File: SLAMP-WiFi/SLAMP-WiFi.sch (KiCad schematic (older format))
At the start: 19 parts

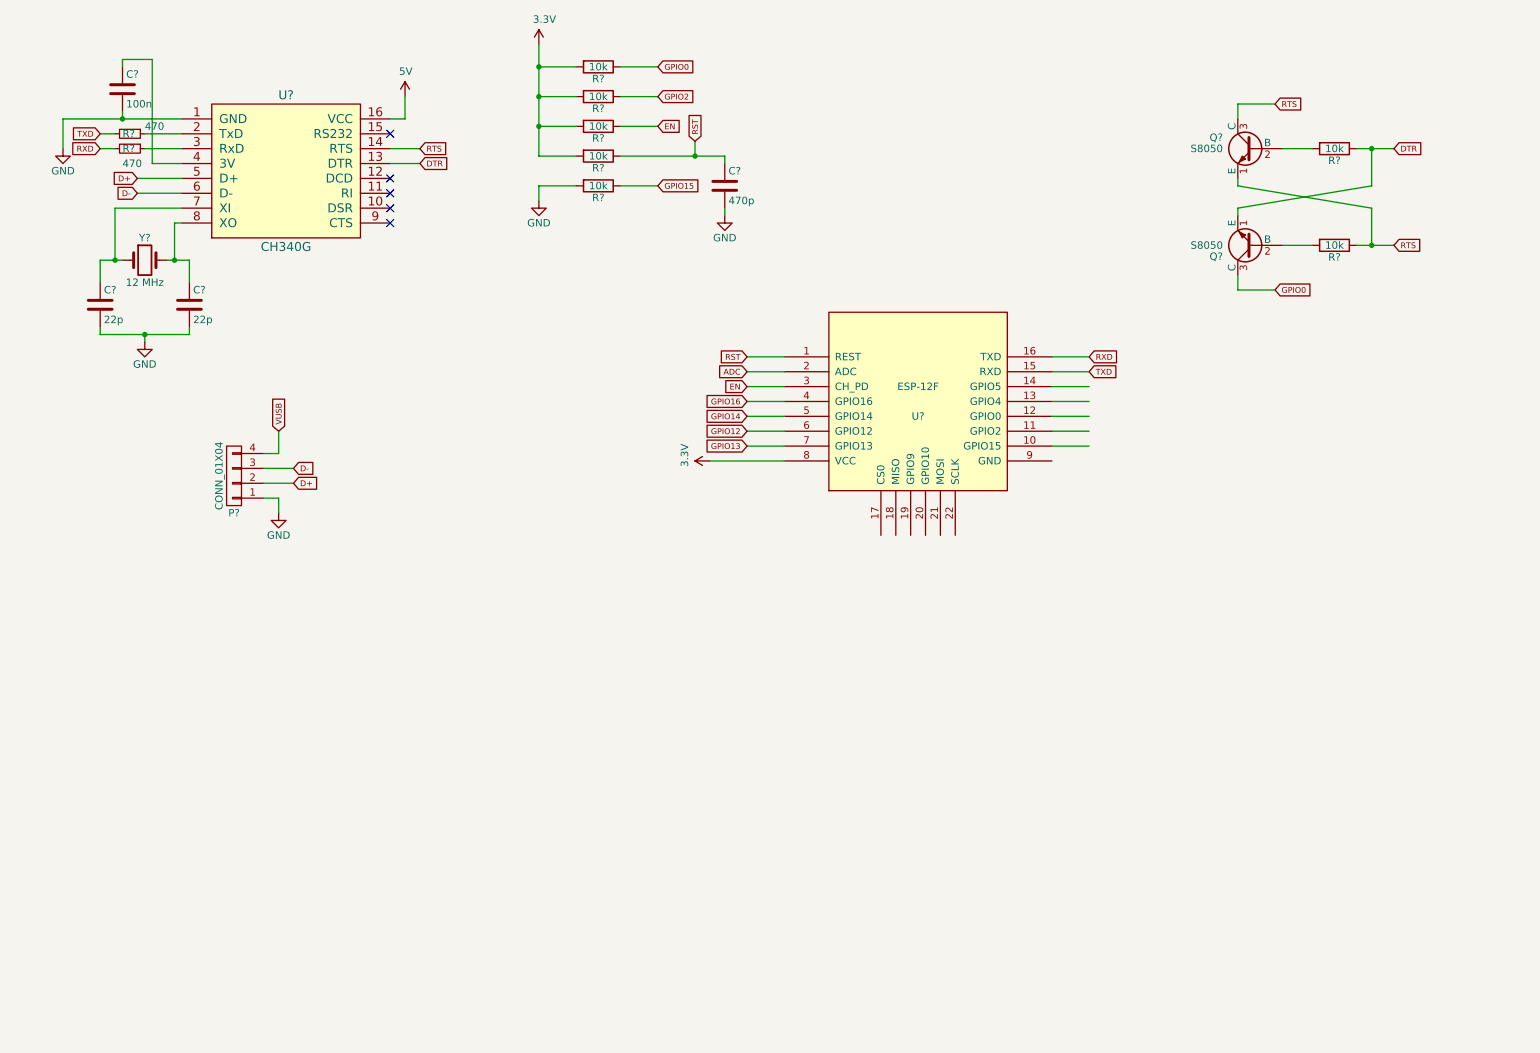
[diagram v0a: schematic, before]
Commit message: Pines de conexionado a las cara terminado, botones terminados
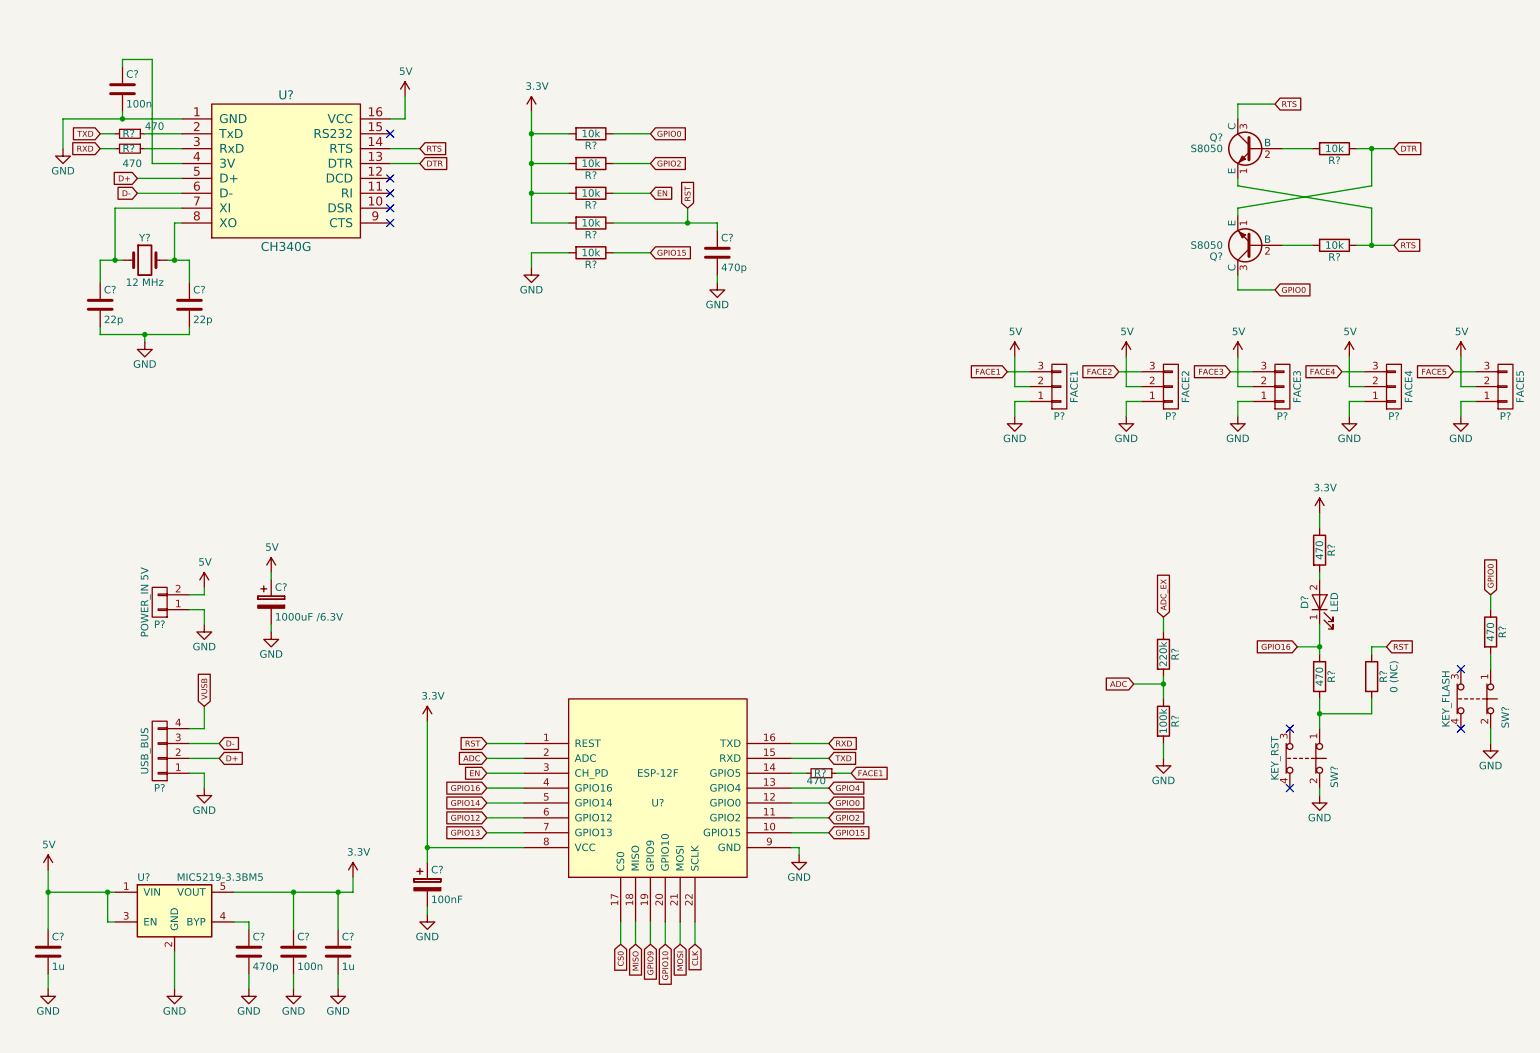
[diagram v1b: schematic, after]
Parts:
- added C?: 470p, symbol C
- added C?: 100n, symbol C
- added C? (x2): 1u, symbol C
- added C?: 100nF, symbol CP
- added C?: 1000uF /6.3V, symbol CP
- added D?: LED, symbol LED
- added P?: POWER_IN 5V, symbol CONN_01X02
- added P?: FACE1, symbol CONN_01X03
- added P?: FACE2, symbol CONN_01X03
- added P?: FACE3, symbol CONN_01X03
- added P?: FACE4, symbol CONN_01X03
- added P?: FACE5, symbol CONN_01X03
- added R?: 100k, symbol R
- added R?: 220k, symbol R
- added R? (x3): 470, symbol R
- added R?: 0 (NC), symbol R
- added R?: 470, symbol R_Small
- added SW?: KEY_RST, symbol SW_Push_Open_Dual
- added SW?: KEY_FLASH, symbol SW_Push_Open_Dual
- added U?: MIC5219-3.3BM5, TO_SOT_Packages_SMD:SOT-23-5, symbol MIC5219-3.3BM5
- P?: value CONN_01X04 -> USB_BUS
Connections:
- net labels added: ADC_EX, CLK, CS0, FACE1, FACE2, FACE3, FACE4, FACE5, GPIO10, GPIO4, GPIO9, MISO, MOSI
- wire segments 79 -> 153
- no-connect marks 5 -> 9
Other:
- moved on the sheet: C?, P?, R?, U?

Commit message: Anotaciones y flags añadidos
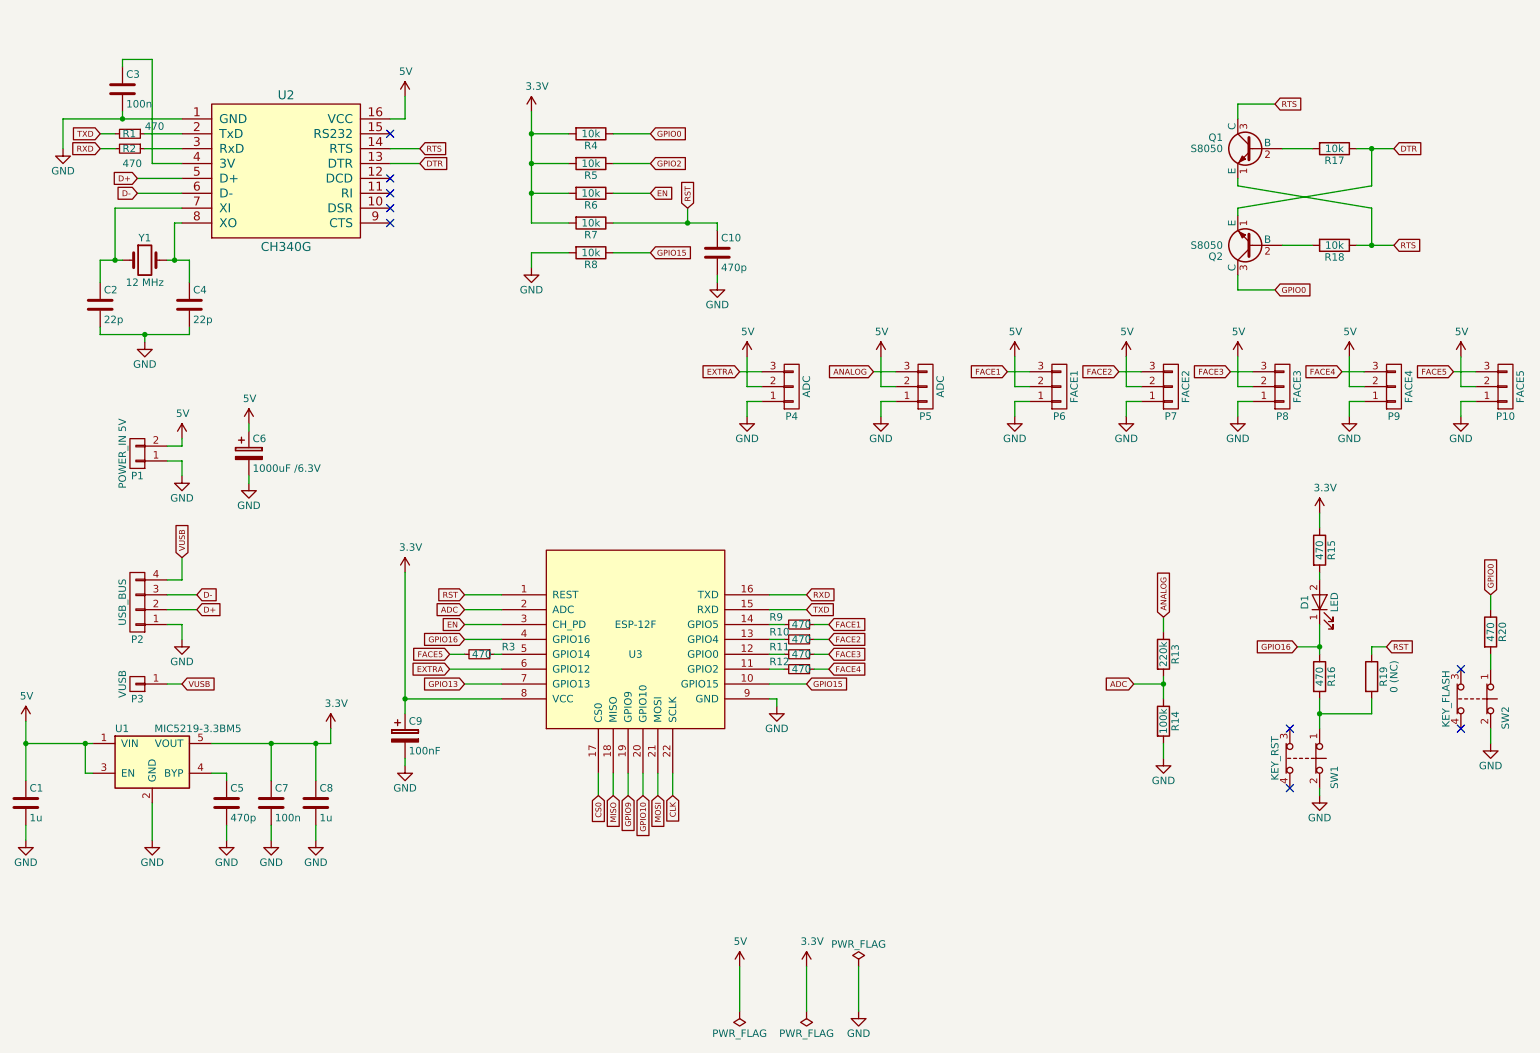
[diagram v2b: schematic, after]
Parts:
- added P3: VUSB, symbol CONN_01X01
- added P4, P5: ADC, symbol CONN_01X03
- added R10, R11, R12, R3: 470, symbol R_Small
- gave numbers to parts that had none: 42
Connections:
- net 5V: now also P4.2 (P2), P5.2 (P2)
- net FACE2: now also R10.1
- net FACE3: now also R11.1
- net FACE4: now also R12.1
- net FACE5: now also R3.2
- net GND: now also P4.1 (P1), P5.1 (P1)
- net GPIO0: no longer U3.12 (GPIO0)
- net GPIO2: no longer U3.11 (GPIO2)
- net VUSB: now also P3.1 (P1)
- net ADC_EX renamed ANALOG
- net ANALOG: now also P5.3 (P3)
- net GPIO12 renamed EXTRA
- net EXTRA: now also P4.3 (P3)
- net GPIO14: no longer names the net of U3.5 (GPIO14)
- net GPIO14: now also R3.1
- net GPIO4: no longer names the net of U3.13 (GPIO4)
- net GPIO4: now also R10.2
- new net: R12.2, U3.11 (GPIO2)
- new net: R11.2, U3.12 (GPIO0)
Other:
- moved on the sheet: C1, C5, C6, C7, C8, C9, P1, P2, R9, U1, U3

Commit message: DRC pasado
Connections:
- net GPIO2 is gone; now on net FACE4: R5.1
- net CLK: no longer names the net of U3.22 (SCLK)
- net CS0: no longer names the net of U3.17 (CS0)
- net GPIO10: no longer names the net of U3.20 (GPIO10)
- net GPIO13: no longer names the net of U3.7 (GPIO13)
- net GPIO9: no longer names the net of U3.19 (GPIO9)
- net MISO: no longer names the net of U3.18 (MISO)
- net MOSI: no longer names the net of U3.21 (MOSI)
- no-connect marks 9 -> 16

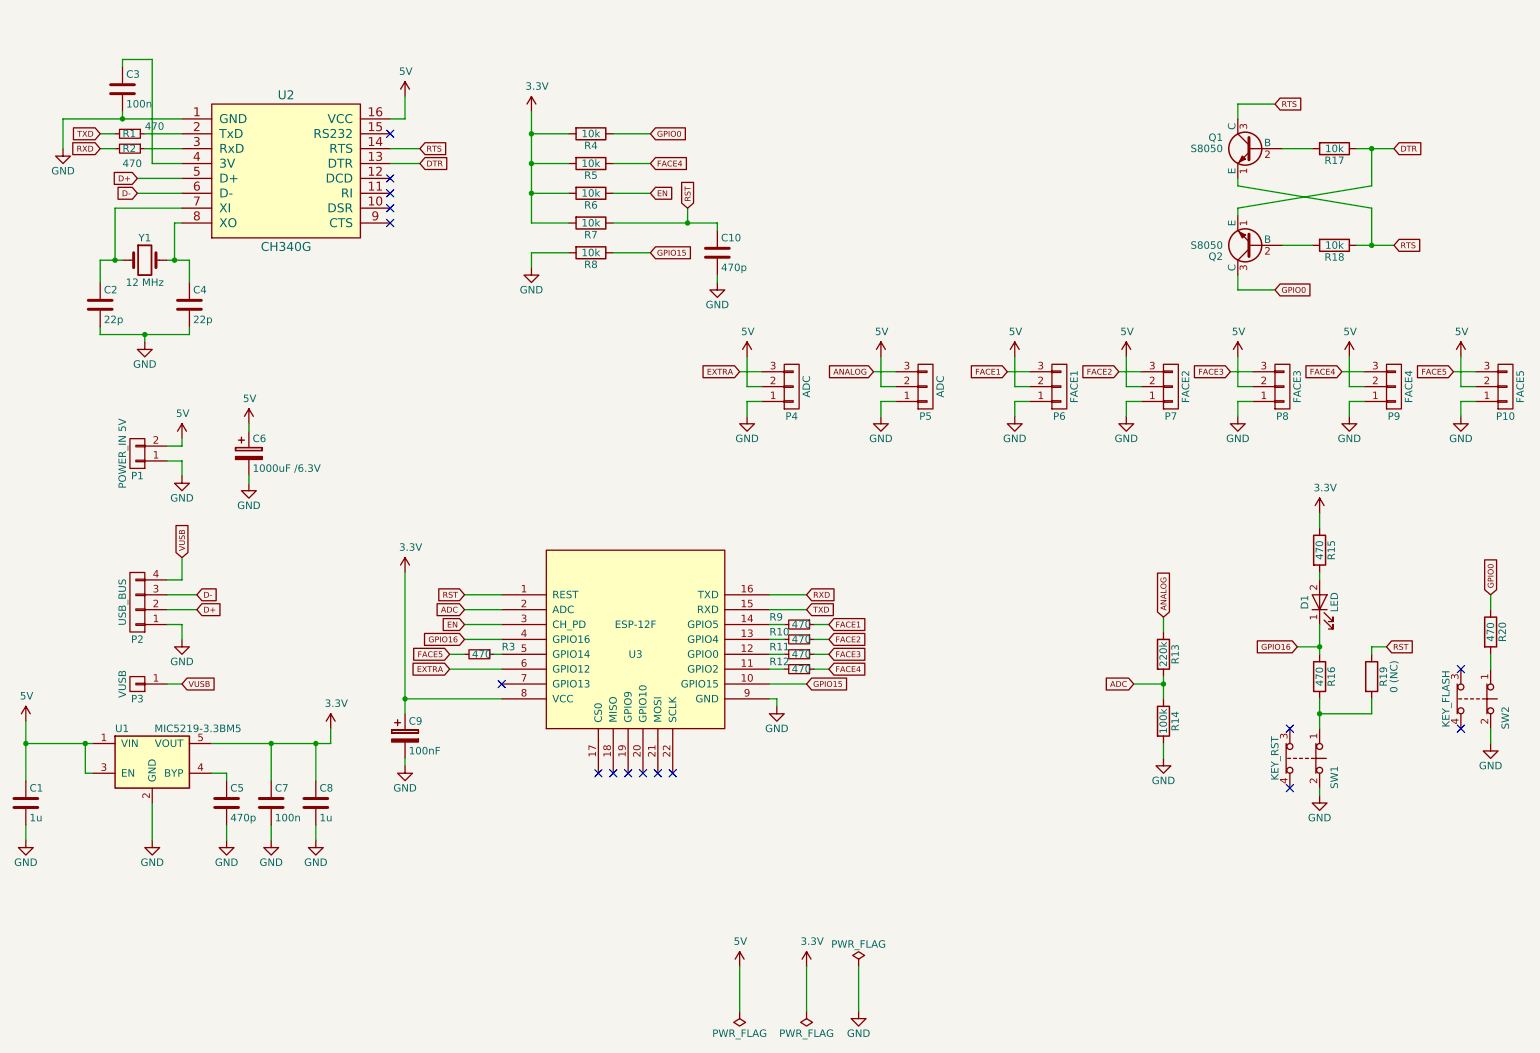
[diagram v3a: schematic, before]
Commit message: Simbolos asignados a sus huellas y netlist exportado
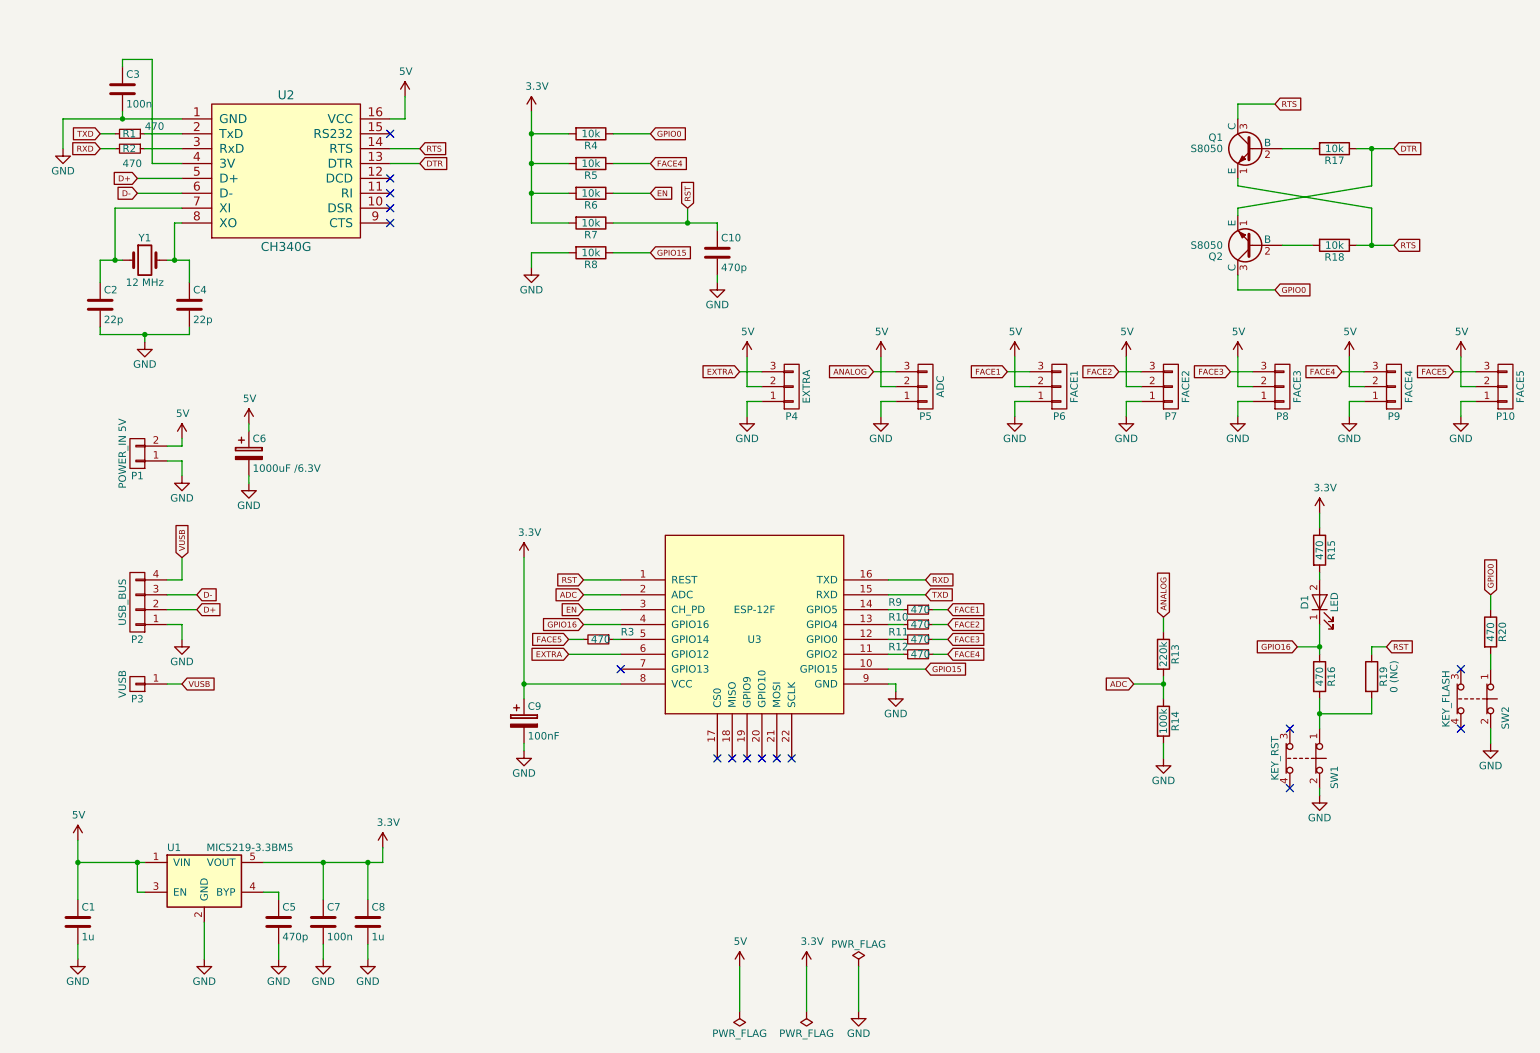
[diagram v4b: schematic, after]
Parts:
- C1, C10, C2, C3, C4, C5, C7, C8: footprint (none) -> Capacitors_SMD:C_0805
- C6: footprint (none) -> Capacitors_THT:CP_Radial_D8.0mm_P3.50mm
- C9: footprint (none) -> Capacitors_SMD:C_1210
- D1: footprint (none) -> LEDs:LED_0805
- P1: footprint (none) -> Connectors_Terminal_Blocks:TerminalBlock_Pheonix_MKDS1.5-2pol
- P10, P5, P6, P7, P8, P9: footprint (none) -> Connectors_JST:JST_XH_B03B-XH-A_03x2.50mm_Straight
- P2: footprint (none) -> Pin_Headers:Pin_Header_Angled_1x04_Pitch2.54mm
- P3: footprint (none) -> Pin_Headers:Pin_Header_Straight_1x01
- P4: value ADC -> EXTRA; footprint (none) -> Connectors_JST:JST_XH_B03B-XH-A_03x2.50mm_Straight
- Q1, Q2: footprint TO-92 -> TO_SOT_Packages_SMD:SOT-23
- R1, R10, R11, R12, R13, R14, R15, R16, R17, R18, R19, R2, R20, R3, R4, R5, R6, R7, R8, R9: footprint (none) -> Resistors_SMD:R_0805
- SW1, SW2: footprint (none) -> Buttons_Switches_THT:SW_PUSH_6mm
- U3: footprint (none) -> ESP8266:ESP-12E
- Y1: footprint (none) -> Crystals:HC-49V
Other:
- moved on the sheet: C1, C5, C7, C8, C9, R10, R11, R12, R3, R9, U1, U3
